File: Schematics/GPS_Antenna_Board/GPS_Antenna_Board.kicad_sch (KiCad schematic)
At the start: 29 parts, among them J1 SATA Conn. (Male), U3 SAM-M10Q, U8 LM66100DCKR

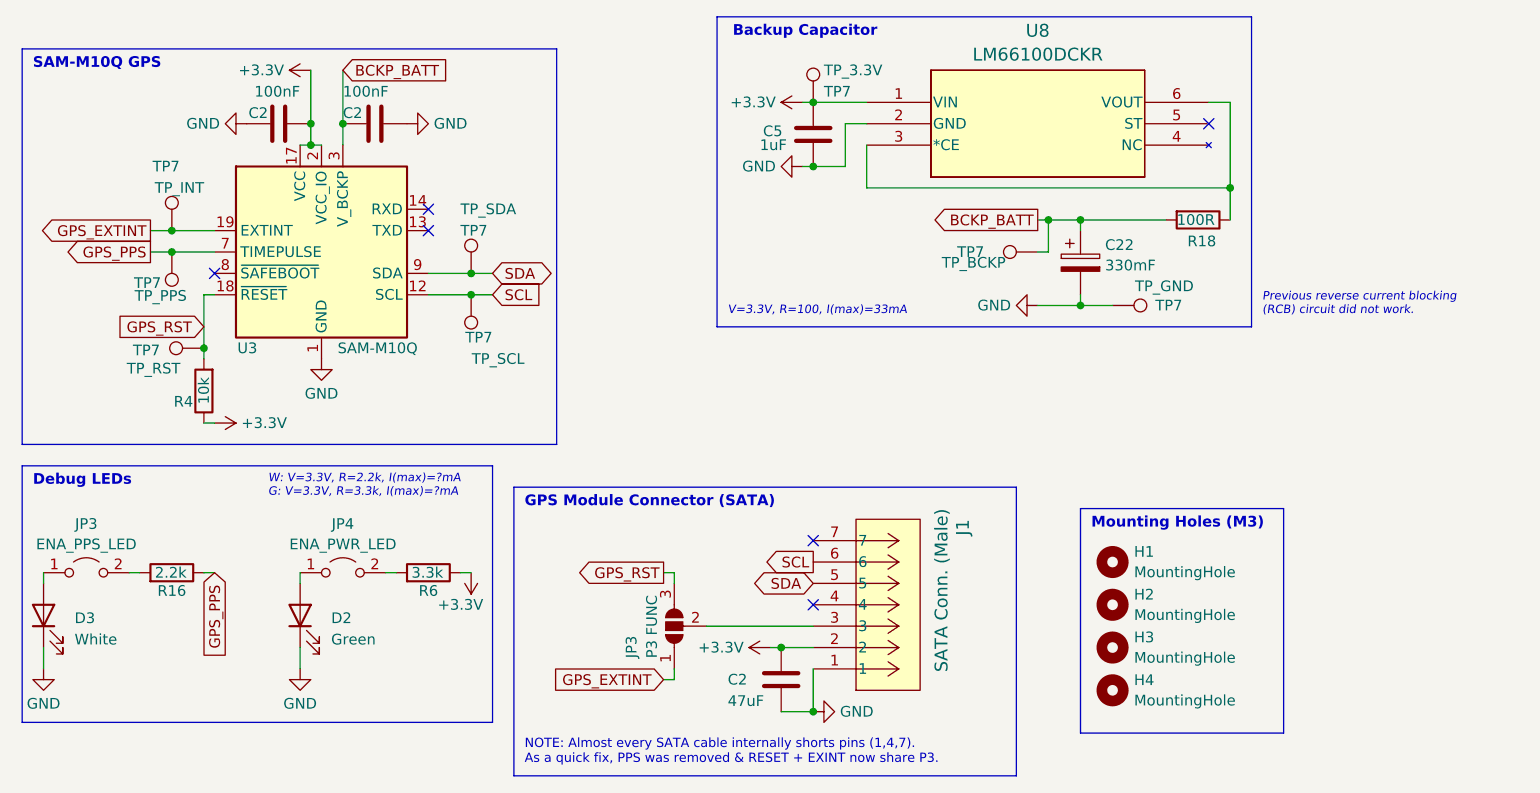
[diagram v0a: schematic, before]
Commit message: Fixed supercap charger RCB
Previous use of LM66100 ideal diode didn't work as, when power was lost, the ideal diode would stop functioning properly and would still let power through. Have swapped to a simple 1N5819 Schottky diode.

Also broke out the TX/RX pins of the GPS for easier external programming, if needed.
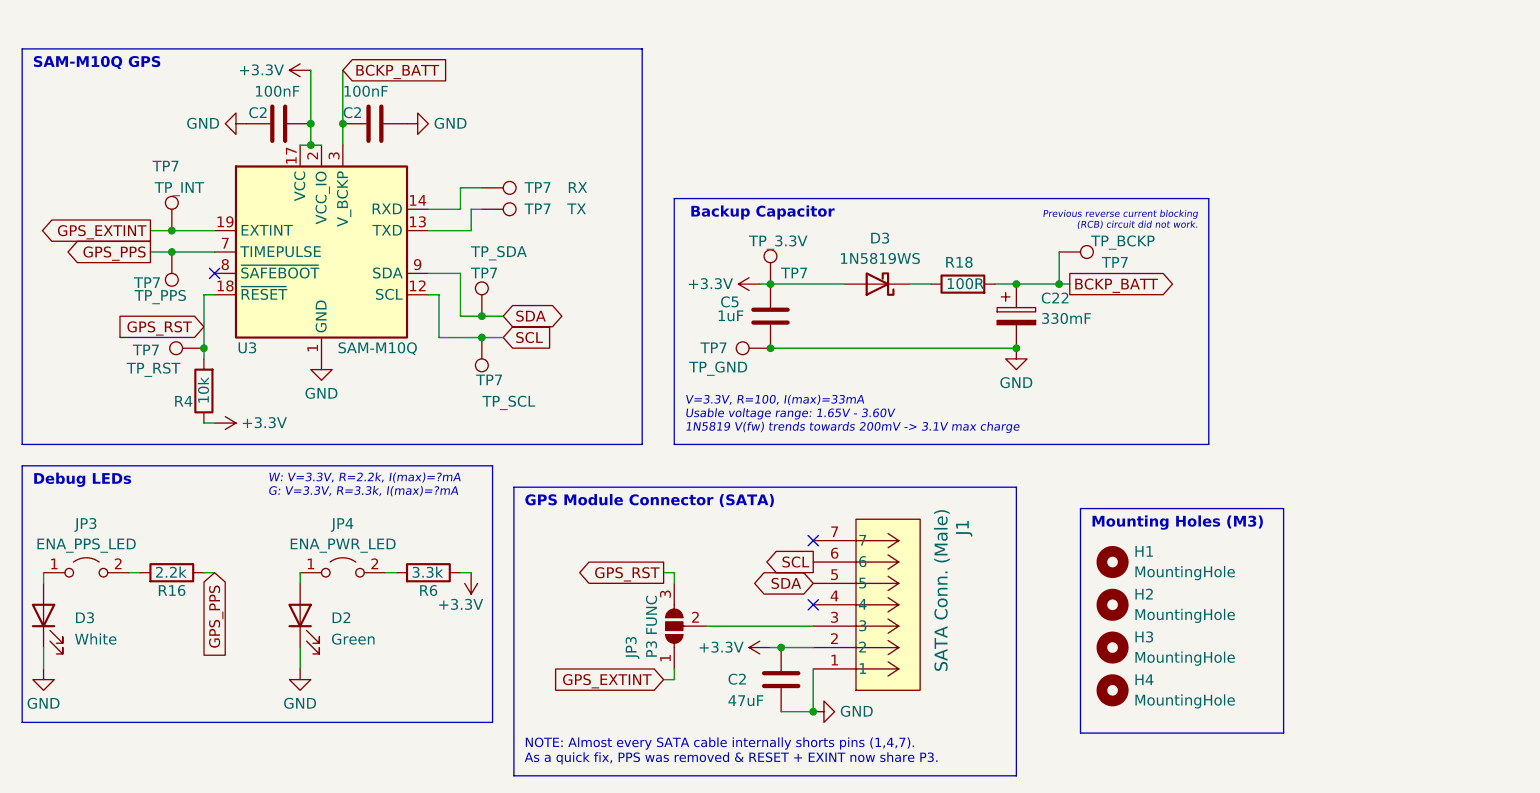
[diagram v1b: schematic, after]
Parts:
- removed U8: LM66100DCKR, LMR66100:SC-70-6_Handsoldering, symbol QRET_Buck_PSU-symbols:LM66100DCKR
- added D3: 1N5819WS, Diode_SMD:D_SOD-323_HandSoldering, symbol Diode:1N5817
- added TP7: TX, TestPoint:TestPoint_Pad_1.5x1.5mm, symbol Connector:TestPoint
- added TP7: RX, TestPoint:TestPoint_Pad_1.5x1.5mm, symbol Connector:TestPoint
- JP3: now left out of the parts list
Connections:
- net +3.3V: now also D3.2 (A)
- net at R18.1: now also D3.1 (K)
- net at U3.13 (TXD): now also TP7.1
- net at U3.14 (RXD): now also TP7.1
- no-connect marks 6 -> 3
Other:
- note added: "V=3.3V, R=100, I(max)=33mA Usable voltage range: 1.65V - 3.60V 1N5819 V(fw) trends towards 200mV -> 3.1V max charge"
- note removed: "V=3.3V, R=100, I(max)=33mA"
- moved on the sheet: C22, C5, R18, TP7

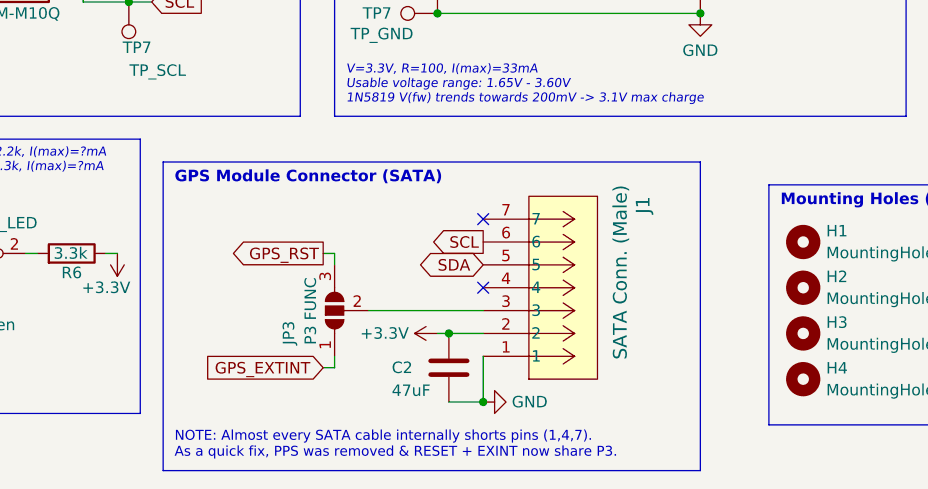
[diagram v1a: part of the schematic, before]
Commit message: Replaced SATA connector on GPS Module+Antenna
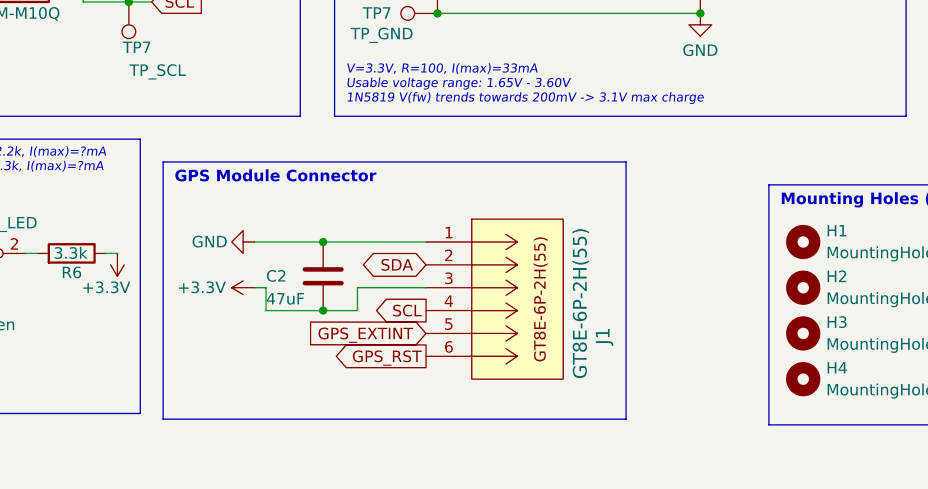
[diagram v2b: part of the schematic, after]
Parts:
- removed J1: SATA Conn. (Male), footprints:CONN_47080-4001_MOL_SATA, symbol CONN_47080-4001_MOL_SATA:470804001
- removed JP3: P3 FUNC, Jumper:SolderJumper-3_P1.3mm_Open_RoundedPad1.0x1.5mm, symbol Jumper:SolderJumper_3_Open
- added J1: GT8E-6P-2H(55), footprints:CONN_GT8E-6P-2H(55), symbol CONN_GT8E-6P-2H(55):GT8E-6P-2H(55)
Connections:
- net +3.3V: now also C2.2, J1.3; no longer C2.1
- net GND: now also C2.1, J1.1; no longer C2.2
- net GPS_EXTINT: now also J1.5
- net GPS_RST: now also J1.6
- net SCL: now also J1.4
- net SDA: now also J1.2
- no-connect marks 3 -> 1
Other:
- note added: "GPS Module Connector"
- note removed: "GPS Module Connector (SATA)"
- note removed: "NOTE: Almost every SATA cable internally shorts pins (1,4,7). As a quick fix, PPS was removed & RESET + EXINT now share P3."
- moved on the sheet: C2

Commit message: Replaced "LCSC" fields with "JLCPCB" fields
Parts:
- C2: JLCPCB (none) -> C14663; LCSC C14663 -> (none)
- C2: JLCPCB (none) -> C16780; LCSC C16780 -> (none)
- C5: JLCPCB (none) -> C15849; LCSC C15849 -> (none)
- D2: JLCPCB (none) -> C2297; LCSC C2297 -> (none)
- D3: JLCPCB (none) -> C34499; LCSC C34499 -> (none)
- D3: JLCPCB (none) -> C191023; LCSC C191023 -> (none)
- R16: JLCPCB (none) -> C4190; LCSC C4190 -> (none)
- R18: JLCPCB (none) -> C22775; LCSC C22775 -> (none)
- R4: JLCPCB (none) -> C25804; LCSC C25804 -> (none)
- R6: JLCPCB (none) -> C22978; LCSC C22978 -> (none)
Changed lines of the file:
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@@
       (effects (font (size 1.27 1.27)) hide)
     )
-    (property "LCSC" "C22978" (at 129.413 113.665 90)
+    (property "JLCPCB" "C22978" (at 129.413 113.665 90)
       (effects (font (size 1.27 1.27)) hide)
     )
@@
       (effects (font (size 1.27 1.27)) hide)
     )
-    (property "LCSC" "C14663" (at 123.19 58.801 90)
+    (property "JLCPCB" "C14663" (at 123.19 58.801 90)
       (effects (font (size 1.27 1.27)) hide)
     )
@@
       (effects (font (size 1.27 1.27)) hide)
     )
-    (property "LCSC" "C2297" (at 121.285 125.349 90)
+    (property "JLCPCB" "C2297" (at 121.285 125.349 90)
       (effects (font (size 1.27 1.27)) hide)
     )
@@
       (effects (font (size 1.27 1.27)) hide)
     )
-    (property "LCSC" "C14663" (at 111.76 65.659 90)
+    (property "JLCPCB" "C14663" (at 111.76 65.659 90)
       (effects (font (size 1.27 1.27)) hide)
     )
@@
       (effects (font (size 1.27 1.27)) hide)
     )
-    (property "LCSC" "C25804" (at 104.648 93.98 90)
+    (property "JLCPCB" "C25804" (at 104.648 93.98 90)
       (effects (font (size 1.27 1.27)) hide)
     )
@@
       (effects (font (size 1.27 1.27)) hide)
     )
-    (property "LCSC" "C22775" (at 193.04 81.28 90)
+    (property "JLCPCB" "C22775" (at 193.04 81.28 90)
       (effects (font (size 1.27 1.27)) hide)
     )
@@
       (effects (font (size 1.27 1.27)) hide)
     )
-    (property "LCSC" "C4190" (at 98.933 113.665 90)
+    (property "JLCPCB" "C4190" (at 98.933 113.665 90)
       (effects (font (size 1.27 1.27)) hide)
     )
@@
       (effects (font (size 1.27 1.27)) hide)
     )
-    (property "LCSC" "C15849" (at 170.18 85.09 0)
+    (property "JLCPCB" "C15849" (at 170.18 85.09 0)
       (effects (font (size 1.27 1.27)) hide)
     )
@@
       (effects (font (size 1.27 1.27)) hide)
     )
-    (property "LCSC" "C34499" (at 90.17 125.349 90)
+    (property "JLCPCB" "C34499" (at 90.17 125.349 90)
       (effects (font (size 1.27 1.27)) hide)
     )
@@
       (effects (font (size 1.27 1.27)) hide)
     )
-    (property "LCSC" "C16780" (at 154.051 118.11 90)
+    (property "JLCPCB" "C16780" (at 154.051 118.11 90)
       (effects (font (size 1.27 1.27)) hide)
     )
@@
       (effects (font (size 1.27 1.27)) hide)
     )
-    (property "LCSC" "C191023" (at 182.88 81.28 0)
-      (effects (font (size 1.27 1.27)) hide)
-    )
+    (property "JLCPCB" "C191023" (at 182.88 81.28 0)
+      (effects (font (size 1.27 1.27)) hide)
+    )

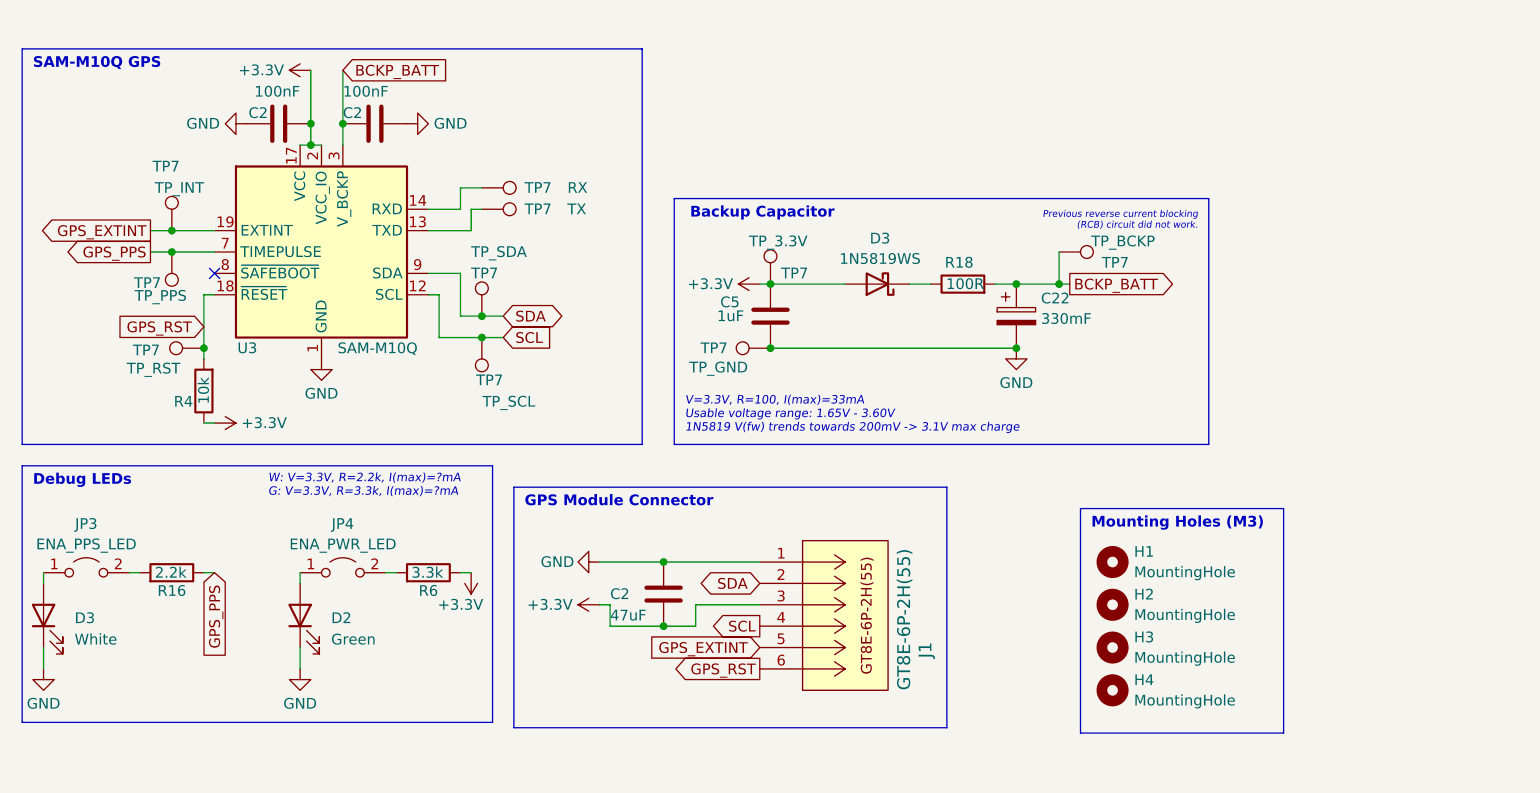
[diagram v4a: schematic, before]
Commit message: Quick adjustments to Antenna PCB
- Added proper silkscreen labels to test points
- Added version number on front of PCB
- Updated version date
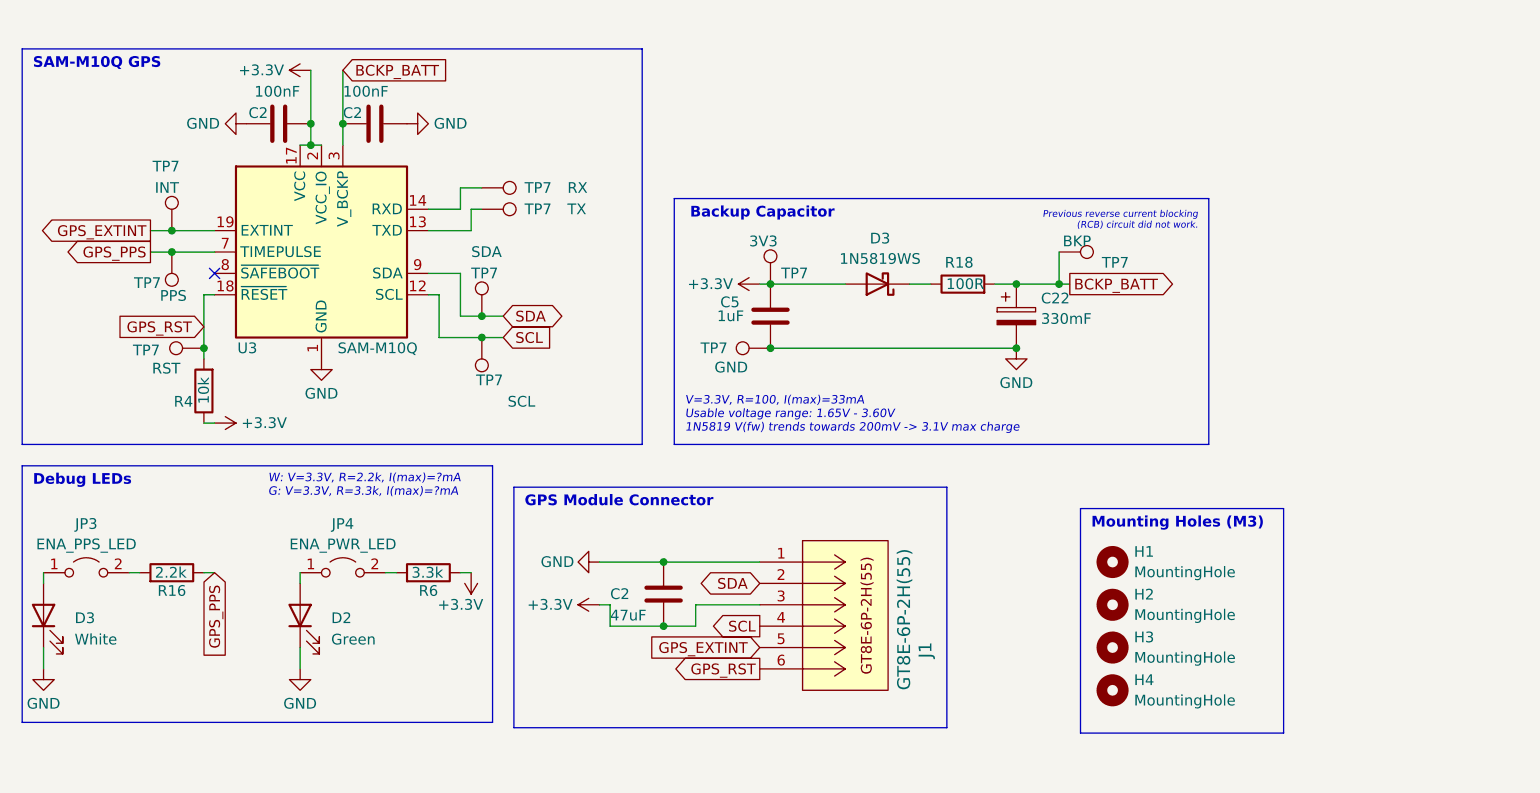
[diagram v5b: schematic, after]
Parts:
- TP7: value TP_3.3V -> 3V3
- TP7: value TP_GND -> GND
- TP7: value TP_PPS -> PPS
- TP7: value TP_SDA -> SDA
- TP7: value TP_BCKP -> BKP
- TP7: value TP_RST -> RST
- TP7: value TP_INT -> INT
- TP7: value TP_SCL -> SCL
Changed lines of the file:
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@@
   (title_block
     (title "QRET 23-24 SRAD GPS Antenna Board")
-    (date "2025-02-16")
+    (date "2025-03-06")
     (rev "V1.2")
     (company "Queen's Rocket Engineering Team")
@@
       (effects (font (size 1.27 1.27)) (justify left))
     )
-    (property "Value" "TP_3.3V" (at 167.64 76.2 0)
+    (property "Value" "3V3" (at 167.64 76.2 0)
       (effects (font (size 1.27 1.27)) (justify left))
     )
@@
       (effects (font (size 1.27 1.27)) (justify left))
     )
-    (property "Value" "TP_GND" (at 167.513 91.186 90)
+    (property "Value" "GND" (at 167.513 91.186 90)
       (effects (font (size 1.27 1.27)) (justify left))
     )
@@
       (effects (font (size 1.27 1.27)) (justify left))
     )
-    (property "Value" "TP_PPS" (at 100.838 82.677 0)
+    (property "Value" "PPS" (at 100.838 82.677 0)
       (effects (font (size 1.27 1.27)) (justify left))
     )
@@
       (effects (font (size 1.27 1.27)) (justify left))
     )
-    (property "Value" "TP_SDA" (at 134.62 77.47 0)
+    (property "Value" "SDA" (at 134.62 77.47 0)
       (effects (font (size 1.27 1.27)) (justify left))
     )
@@
       (effects (font (size 1.27 1.27)) (justify left))
     )
-    (property "Value" "TP_BCKP" (at 208.28 76.2 90)
-      (effects (font (size 1.27 1.27)) (justify left))
+    (property "Value" "BKP" (at 208.28 76.2 90)
+      (effects (font (size 1.27 1.27)) (justify right))
     )
     (property "Footprint" "TestPoint:TestPoint_Pad_1.5x1.5mm" (at 204.47 72.39 0)
@@
       (effects (font (size 1.27 1.27)) (justify left))
     )
-    (property "Value" "TP_RST" (at 100.076 91.313 90)
+    (property "Value" "RST" (at 100.076 91.313 90)
       (effects (font (size 1.27 1.27)) (justify left))
     )
@@
       (effects (font (size 1.27 1.27)) (justify left))
     )
-    (property "Value" "TP_INT" (at 97.028 69.85 0)
+    (property "Value" "INT" (at 97.028 69.85 0)
       (effects (font (size 1.27 1.27)) (justify left))
     )
@@
       (effects (font (size 1.27 1.27)) (justify left))
     )
-    (property "Value" "TP_SCL" (at 142.24 95.25 0)
-      (effects (font (size 1.27 1.27)) (justify left))
-    )
+    (property "Value" "SCL" (at 142.24 95.25 0)
+      (effects (font (size 1.27 1.27)) (justify left))
+    )

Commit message: Added missing part numbers
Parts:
- J1: Digikey (none) -> 26-GT8E-6P-2H(55)CT-ND
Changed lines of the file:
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@@
       (effects (font (size 1.27 1.27) italic) hide)
+    )
+    (property "Digikey" "26-GT8E-6P-2H(55)CT-ND" (at 168.91 114.3 90)
+      (effects (font (size 1.27 1.27)) hide)
     )
     (pin "1")
